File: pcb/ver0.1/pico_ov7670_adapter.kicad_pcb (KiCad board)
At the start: 2 copper layers, 95 x 46 mm, 12 parts, among them J1 Conn_02x06_Odd_Even, SW1 SW_Push, U1 CAMERA-OV7670, U2 RASPBERRY_PI_PICO_W

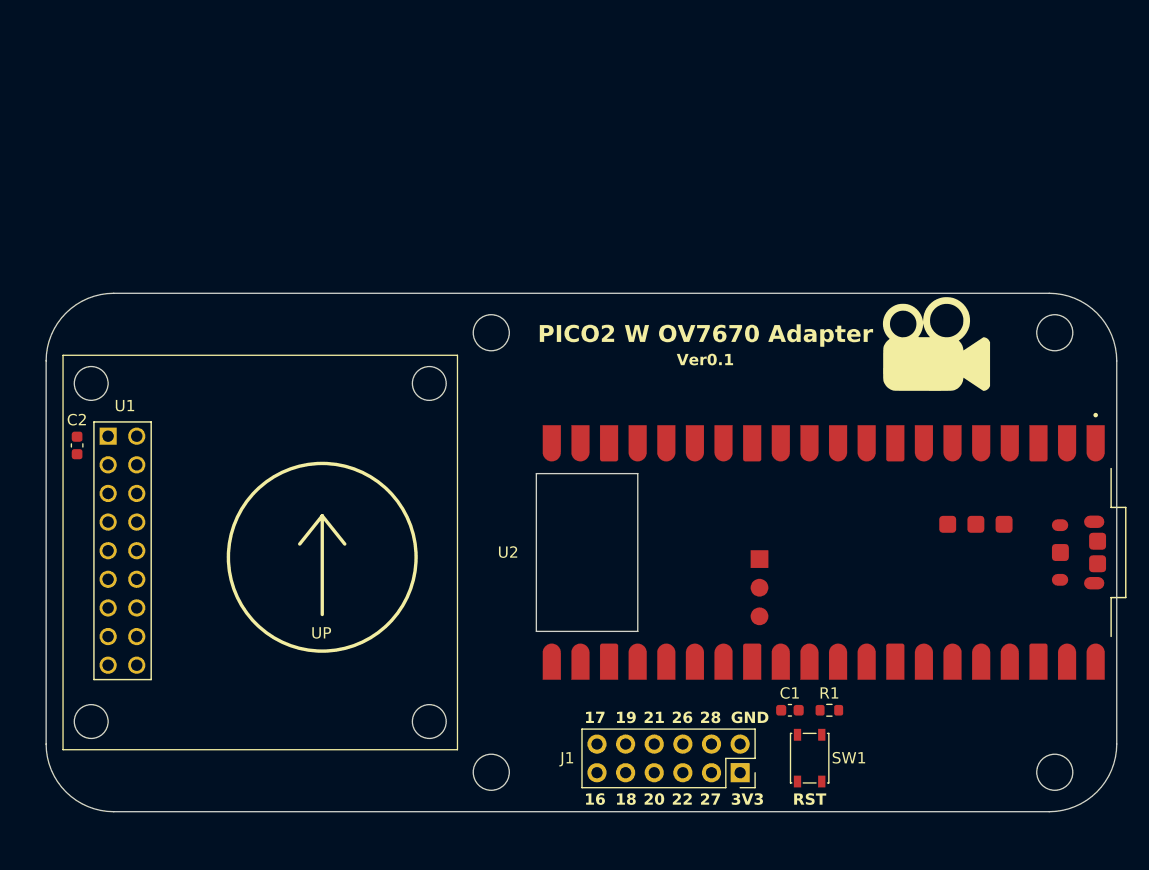
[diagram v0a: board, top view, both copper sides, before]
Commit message: footprints updated
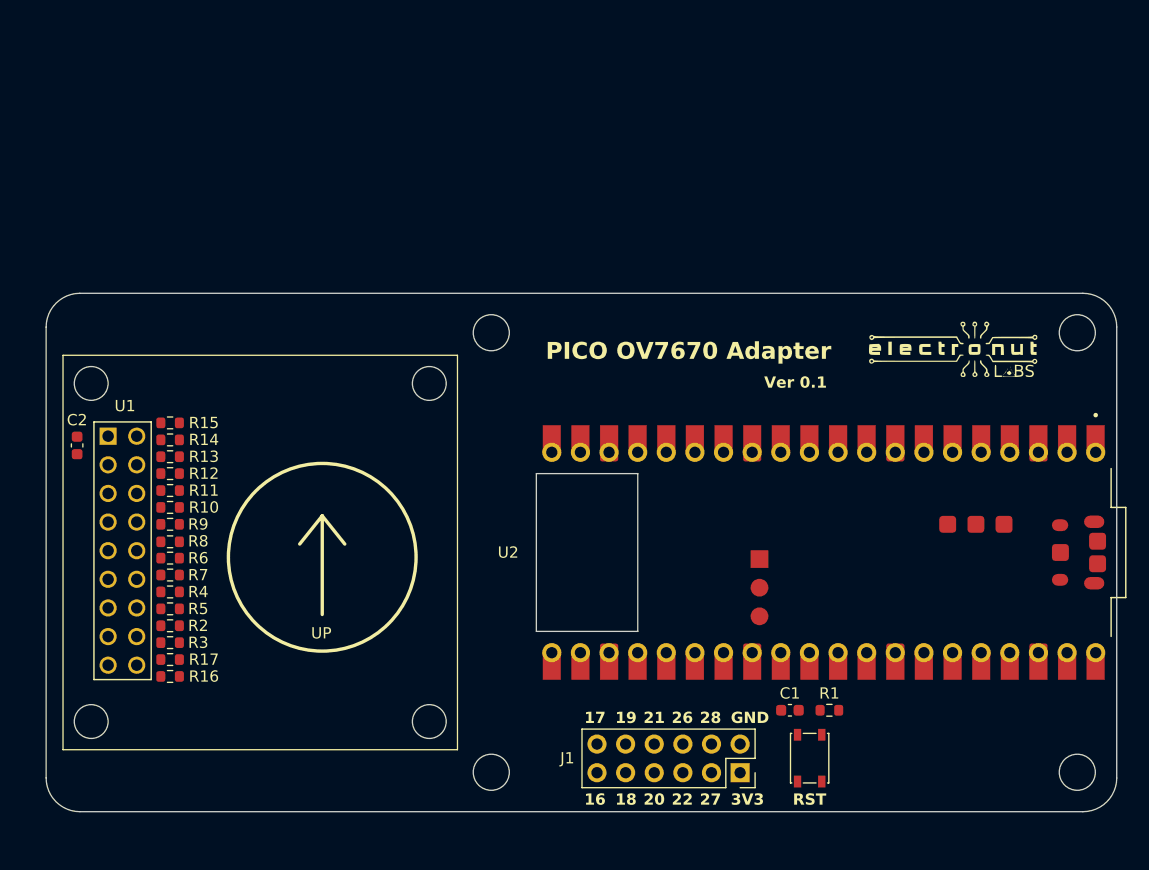
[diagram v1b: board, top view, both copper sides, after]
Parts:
- removed the G*** at (169.0, 78.5)
- added G***: LOGO, pico_ov7670_adapter:logo, F.Cu at (170.5, 79.0)
- added R10: 22R, Resistor_SMD:R_0603_1608Metric, F.Cu at (101.0, 93.0)
- added R11: 22R, Resistor_SMD:R_0603_1608Metric, F.Cu at (101.0, 91.5)
- added R12: 22R, Resistor_SMD:R_0603_1608Metric, F.Cu at (101.0, 90.0)
- added R13: 22R, Resistor_SMD:R_0603_1608Metric, F.Cu at (101.0, 88.5)
- added R14: 22R, Resistor_SMD:R_0603_1608Metric, F.Cu at (101.0, 87.0)
- added R15: 22R, Resistor_SMD:R_0603_1608Metric, F.Cu at (101.0, 85.5)
- added R16: 22R, Resistor_SMD:R_0603_1608Metric, F.Cu at (101.0, 108.0)
- added R17: 22R, Resistor_SMD:R_0603_1608Metric, F.Cu at (101.0, 106.5)
- added R2: 22R, Resistor_SMD:R_0603_1608Metric, F.Cu at (101.0, 103.5)
- added R3: 22R, Resistor_SMD:R_0603_1608Metric, F.Cu at (101.0, 105.0)
- added R4: 22R, Resistor_SMD:R_0603_1608Metric, F.Cu at (101.0, 100.5)
- added R5: 22R, Resistor_SMD:R_0603_1608Metric, F.Cu at (101.0, 102.0)
- added R6: 22R, Resistor_SMD:R_0603_1608Metric, F.Cu at (101.0, 97.5)
- added R7: 22R, Resistor_SMD:R_0603_1608Metric, F.Cu at (101.0, 99.0)
- added R8: 22R, Resistor_SMD:R_0603_1608Metric, F.Cu at (101.0, 96.0)
- added R9: 22R, Resistor_SMD:R_0603_1608Metric, F.Cu at (101.0, 94.5)
- moved H3 2.00 mm to (181.5, 77.5)
- moved H4 2.00 mm to (181.5, 116.5)
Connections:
- U2 pad 1: OV_D0_PICO_IO0 -> Net-(U2-UART0_TX/I2C0_SDA/SPI0_RX/GP0)
- U2 pad 10: OV_D7_PICO_IO7 -> Net-(U2-I2C1_SCL/SPI0_TX/GP7)
- U2 pad 11: OV_XCLK_PICO_IO8 -> Net-(U2-UART1_TX/I2C0_SDA/SPI1_RX/GP8)
- U2 pad 12: OV_PCLK_PICO_IO9 -> Net-(U2-UART1_RX/I2C0_SCL/SPI1_CSN/GP9)
- U2 pad 14: OV_VSYNC_PICO_IO10 -> Net-(U2-I2C1_SDA/SPI1_SCK/GP10)
- U2 pad 15: OV_HREF_PICO_IO11 -> Net-(U2-I2C1_SCL/SPI1_TX/GP11)
- U2 pad 16: OV_SDA_PICO_IO12_SDA -> Net-(U2-UART0_TX/I2C0_SDA/SPI1_RX/GP12)
- U2 pad 17: OV_SCL_PICO_IO13_SCL -> Net-(U2-UART0_RX/I2C0_SCL/SPI1_CSN/GP13)
- U2 pad 19: OV_RST_PICO_IO14 -> Net-(U2-I2C1_SDA/SPI1_SCK/GP14)
- U2 pad 2: OV_D1_PICO_IO1 -> Net-(U2-UART0_RX/I2C0_SCL/SPI0_CSN/GP1)
- U2 pad 20: OV_PWDWNPICO_IO15 -> Net-(U2-I2C1_SCL/SPI1_TX/GP15)
- U2 pad 4: OV_D2_PICO_IO2 -> Net-(U2-I2C1_SDA/SPI0_SCK/GP2)
- U2 pad 5: OV_D3_PICO_IO3 -> Net-(U2-I2C1_SCL/SPI0_TX/GP3)
- U2 pad 6: OV_D4_PICO_IO4 -> Net-(U2-UART1_TX/I2C0_SDA/SPI0_RX/GP4)
- U2 pad 7: OV_D5_PICO_IO5 -> Net-(U2-UART1_RX/I2C0_SCL/SPI0_CSN/GP5)
- U2 pad 9: OV_D6_PICO_IO6 -> Net-(U2-I2C1_SDA/SPI0_SCK/GP6)
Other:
- outline, holes or cut-outs redrawn
- board text added: "PICO OV7670 Adapter"
- board text added: "Ver 0.1"
- board text removed: "PICO2 W OV7670 Adapter"
- board text removed: "Ver0.1"

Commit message: layout updated
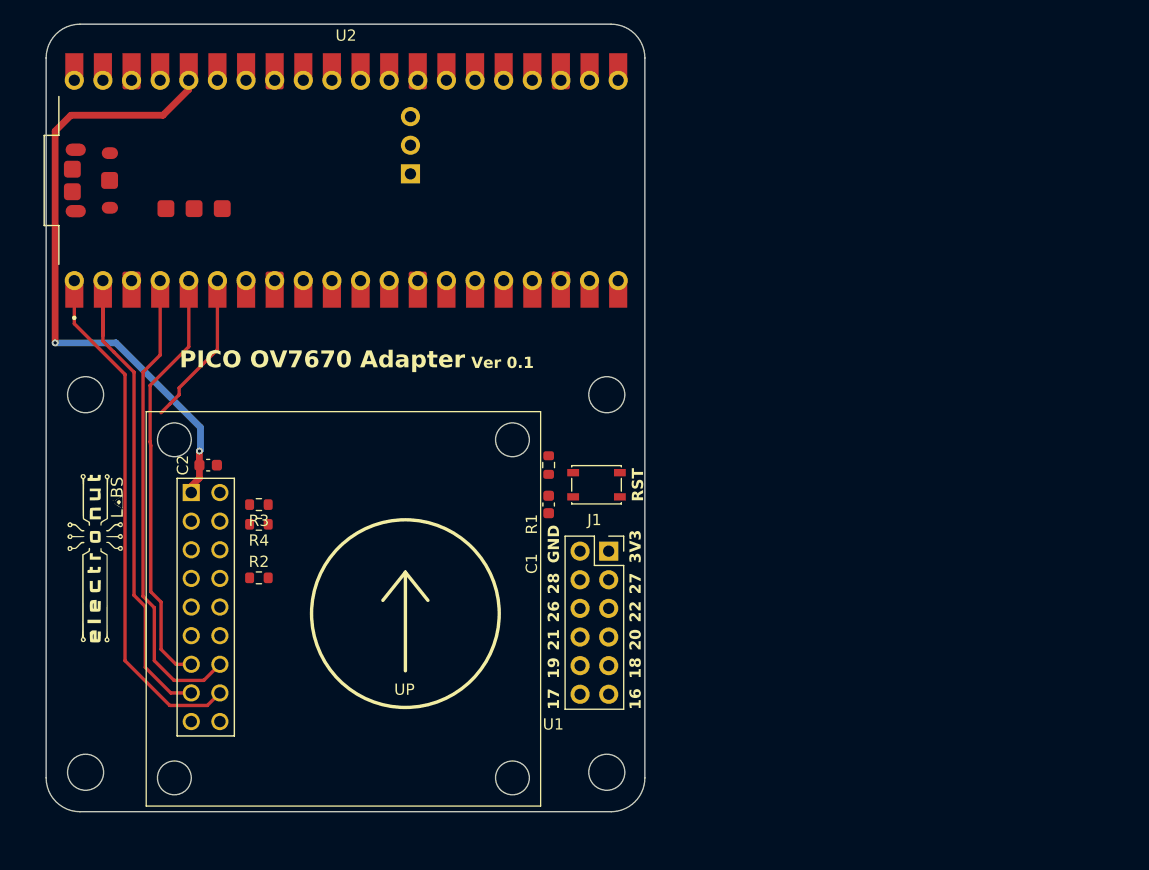
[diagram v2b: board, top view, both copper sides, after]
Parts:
- removed R10, R11, R12, R13, R14, R15, R16, R17, R5, R6, R7, R8, R9: 22R, Resistor_SMD:R_0603_1608Metric
- R3, R4: value 22R -> 10K
- moved H3 88.2 mm to (93.5, 83.0)
- moved H4 88.0 mm to (93.5, 116.5)
- moved G*** 78.3 mm to (94.4, 97.5), turned to 90 degrees
- moved U2 53.7 mm to (116.6, 64.0), turned to 90 degrees
- moved R1 33.1 mm to (134.6, 89.2), turned to -90 degrees
- moved SW1 30.8 mm to (138.8, 91.0), turned to 0 degrees
- moved C1 28.1 mm to (134.6, 92.7), turned to -90 degrees
- moved J1 22.9 mm to (139.9, 96.9), turned to 0 degrees
- moved R3 14.6 mm to (108.9, 92.8), turned to 180 degrees
- moved C2 11.8 mm to (104.4, 89.2), turned to 0 degrees
- moved H1 11.6 mm to (139.8, 83.0)
- moved H2 10.2 mm to (139.8, 116.5)
- moved R4 9.90 mm to (108.9, 94.5), turned to 180 degrees
- moved R2 8.95 mm to (108.9, 99.2)
- moved U1 8.91 mm to (116.4, 102.0)
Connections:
- R2 pad 1: OV_D0_PICO_IO0 -> OV_XCLK_PICO_IO8
- R2 pad 2: Net-(U2-UART0_TX/I2C0_SDA/SPI0_RX/GP0) -> Net-(U2-UART1_TX/I2C0_SDA/SPI1_RX/GP8)
- R3 pad 1: OV_D1_PICO_IO1 -> +3V3
- R3 pad 2: Net-(U2-UART0_RX/I2C0_SCL/SPI0_CSN/GP1) -> OV_SCL_PICO_IO13_SCL
- R4 pad 1: OV_D2_PICO_IO2 -> +3V3
- R4 pad 2: Net-(U2-I2C1_SDA/SPI0_SCK/GP2) -> OV_SDA_PICO_IO12_SDA
- U2 pad 1: Net-(U2-UART0_TX/I2C0_SDA/SPI0_RX/GP0) -> OV_D0_PICO_IO0
- U2 pad 10: Net-(U2-I2C1_SCL/SPI0_TX/GP7) -> OV_D7_PICO_IO7
- U2 pad 12: Net-(U2-UART1_RX/I2C0_SCL/SPI1_CSN/GP9) -> OV_PCLK_PICO_IO9
- U2 pad 14: Net-(U2-I2C1_SDA/SPI1_SCK/GP10) -> OV_VSYNC_PICO_IO10
- U2 pad 15: Net-(U2-I2C1_SCL/SPI1_TX/GP11) -> OV_HREF_PICO_IO11
- U2 pad 16: Net-(U2-UART0_TX/I2C0_SDA/SPI1_RX/GP12) -> OV_SDA_PICO_IO12_SDA
- U2 pad 17: Net-(U2-UART0_RX/I2C0_SCL/SPI1_CSN/GP13) -> OV_SCL_PICO_IO13_SCL
- U2 pad 19: Net-(U2-I2C1_SDA/SPI1_SCK/GP14) -> OV_RST_PICO_IO14
- U2 pad 2: Net-(U2-UART0_RX/I2C0_SCL/SPI0_CSN/GP1) -> OV_D1_PICO_IO1
- U2 pad 20: Net-(U2-I2C1_SCL/SPI1_TX/GP15) -> OV_PWDWNPICO_IO15
- U2 pad 4: Net-(U2-I2C1_SDA/SPI0_SCK/GP2) -> OV_D2_PICO_IO2
- U2 pad 5: Net-(U2-I2C1_SCL/SPI0_TX/GP3) -> OV_D3_PICO_IO3
- U2 pad 6: Net-(U2-UART1_TX/I2C0_SDA/SPI0_RX/GP4) -> OV_D4_PICO_IO4
- U2 pad 7: Net-(U2-UART1_RX/I2C0_SCL/SPI0_CSN/GP5) -> OV_D5_PICO_IO5
- U2 pad 9: Net-(U2-I2C1_SDA/SPI0_SCK/GP6) -> OV_D6_PICO_IO6
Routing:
- net +3V3: track 0.00 -> 56.0 mm, vias 0 -> 2
- net OV_D0_PICO_IO0: track 0.00 -> 45.3 mm
- net OV_D1_PICO_IO1: track 0.00 -> 45.0 mm
- net OV_D2_PICO_IO2: track 0.00 -> 41.1 mm
- net OV_D3_PICO_IO3: track 0.00 -> 37.0 mm
- net OV_D4_PICO_IO4: track 0.00 -> 13.8 mm
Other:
- board size 95 x 46 mm -> 53.1 x 69.9 mm

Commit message: basic routing completed
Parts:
- added C3: 0.1uF, Capacitor_SMD:C_0603_1608Metric, F.Cu at (136.2, 88.5)
- added R5: 10K, Resistor_SMD:R_0603_1608Metric, F.Cu at (134.8, 88.5)
- added SW2: SW_Push, Button_Switch_SMD:SW_SPST_PTS810, F.Cu at (140.0, 88.5)
- J1: value Conn_02x06_Odd_Even -> GPIO Header; footprint Connector_PinSocket_2.54mm:PinSocket_2x06_P2.54mm_Vertical -> Connector_PinHeader_2.54mm:PinHeader_2x05_P2.54mm_Vertical
- moved R1 5.76 mm to (134.8, 95.0), turned to 90 degrees
- moved J1 4.55 mm to (137.5, 100.7)
- moved SW1 3.94 mm to (140.0, 94.8)
- moved R4 3.00 mm to (109.0, 91.5)
- moved C1 2.80 mm to (136.2, 95.0)
- moved R3 1.75 mm to (109.0, 94.5)
- moved H2 0.35 mm to (140.0, 116.8)
- moved H3 0.35 mm to (93.2, 83.2)
- moved H4 0.35 mm to (93.2, 116.8)
- moved H1 0.25 mm to (140.0, 83.0)
- moved R2 0.12 mm to (109.0, 99.2)
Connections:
- net Net-(U2-~{RUN}) renamed /PICO_RESET
- J1 pad 10: /PICO_IO19 -> /PICO_IO27
- J1 pad 3: /PICO_IO27 -> GND
- J1 pad 4: /PICO_IO28 -> /PICO_IO19
- J1 pad 5: /PICO_IO22 -> /PICO_IO21
- J1 pad 6: /PICO_IO26 -> /PICO_IO20
- J1 pad 7: /PICO_IO20 -> /PICO_IO26
- J1 pad 8: /PICO_IO21 -> /PICO_IO22
- J1 pad 9: /PICO_IO18 -> /PICO_IO28
- R2 pad 2: Net-(U2-UART1_TX/I2C0_SDA/SPI1_RX/GP8) -> Net-(U2-UART0_TX/I2C0_SDA/SPI1_RX/GP12)
- U1 pad 18: OV_PWDWNPICO_IO15 -> OV_PWDWN_PICO_IO15
- U2 pad 11: Net-(U2-UART1_TX/I2C0_SDA/SPI1_RX/GP8) -> OV_SDA_PICO_IO12_SDA
- U2 pad 12: OV_PCLK_PICO_IO9 -> OV_SCL_PICO_IO13_SCL
- U2 pad 14: OV_VSYNC_PICO_IO10 -> OV_HREF_PICO_IO11
- U2 pad 15: OV_HREF_PICO_IO11 -> OV_VSYNC_PICO_IO10
- U2 pad 16: OV_SDA_PICO_IO12_SDA -> Net-(U2-UART0_TX/I2C0_SDA/SPI1_RX/GP12)
- U2 pad 17: OV_SCL_PICO_IO13_SCL -> OV_PCLK_PICO_IO9
- U2 pad 19: OV_RST_PICO_IO14 -> OV_PWDWN_PICO_IO15
- U2 pad 20: OV_PWDWNPICO_IO15 -> OV_RST_PICO_IO14
- U2 pad 21: /PICO_IO16 -> unconnected-(U2-UART0_TX/I2C0_SDA/SPI0_RX/GP16-Pad21)
- U2 pad 22: /PICO_IO17 -> unconnected-(U2-UART0_RX/I2C0_SCL/SPI0_CSN/GP17-Pad22)
- U2 pad 24: /PICO_IO18 -> /USER_Button
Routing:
- net +3V3: track 56.0 -> 162.8 mm, vias 2 -> 7
- net /PICO_IO28: track 0.00 -> 81.5 mm
- net /PICO_IO27: track 0.00 -> 77.8 mm
- net /PICO_IO26: track 0.00 -> 71.5 mm
- net /PICO_IO22: track 0.00 -> 71.4 mm
- net OV_RST_PICO_IO14: track 0.00 -> 66.9 mm
- net /PICO_RESET: track 0.00 -> 64.7 mm, vias 0 -> 1
- net /PICO_IO21: track 0.00 -> 63.1 mm
- net /PICO_IO20: track 0.00 -> 62.3 mm
- net OV_PWDWN_PICO_IO15: track 0.00 -> 61.9 mm
- net /PICO_IO19: track 0.00 -> 60.8 mm
- net OV_PCLK_PICO_IO9: track 0.00 -> 52.1 mm
- net OV_D6_PICO_IO6: track 0.00 -> 43.0 mm
- net OV_VSYNC_PICO_IO10: track 0.00 -> 42.2 mm
- net /USER_Button: track 0.00 -> 39.9 mm, vias 0 -> 1
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- added copper zone on B.Cu, net GND
- added copper zone on F.Cu, net GND
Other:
- outline, holes or cut-outs redrawn
- board text added: "PICO 2 OV7670 Adapter"
- board text added: "U.B"
- board text removed: "16"
- board text removed: "17"
- board text removed: "18"
- board text removed: "PICO OV7670 Adapter"
- board text removed: "UP"

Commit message: routing completed
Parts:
- turned R5 to 90 degrees
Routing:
- net OV_HREF_PICO_IO11: track 36.0 -> 39.3 mm
- net OV_VSYNC_PICO_IO10: track 42.2 -> 45.2 mm
- net /PICO_IO19: track 60.8 -> 58.1 mm
- net +3V3: track 162.8 -> 165.1 mm
- net Net-(U2-UART0_TX/I2C0_SDA/SPI1_RX/GP12): track 39.0 -> 40.7 mm
- net /PICO_RESET: track 64.7 -> 66.2 mm
- net /USER_Button: track 39.9 -> 41.4 mm
- net OV_RST_PICO_IO14: track 66.9 -> 68.4 mm
- net OV_D6_PICO_IO6: track 43.0 -> 41.9 mm
- net OV_PCLK_PICO_IO9: track 52.1 -> 53.0 mm
- net GND: vias 13 -> 9
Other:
- board text added: "USR"
- board text removed: "U.B"

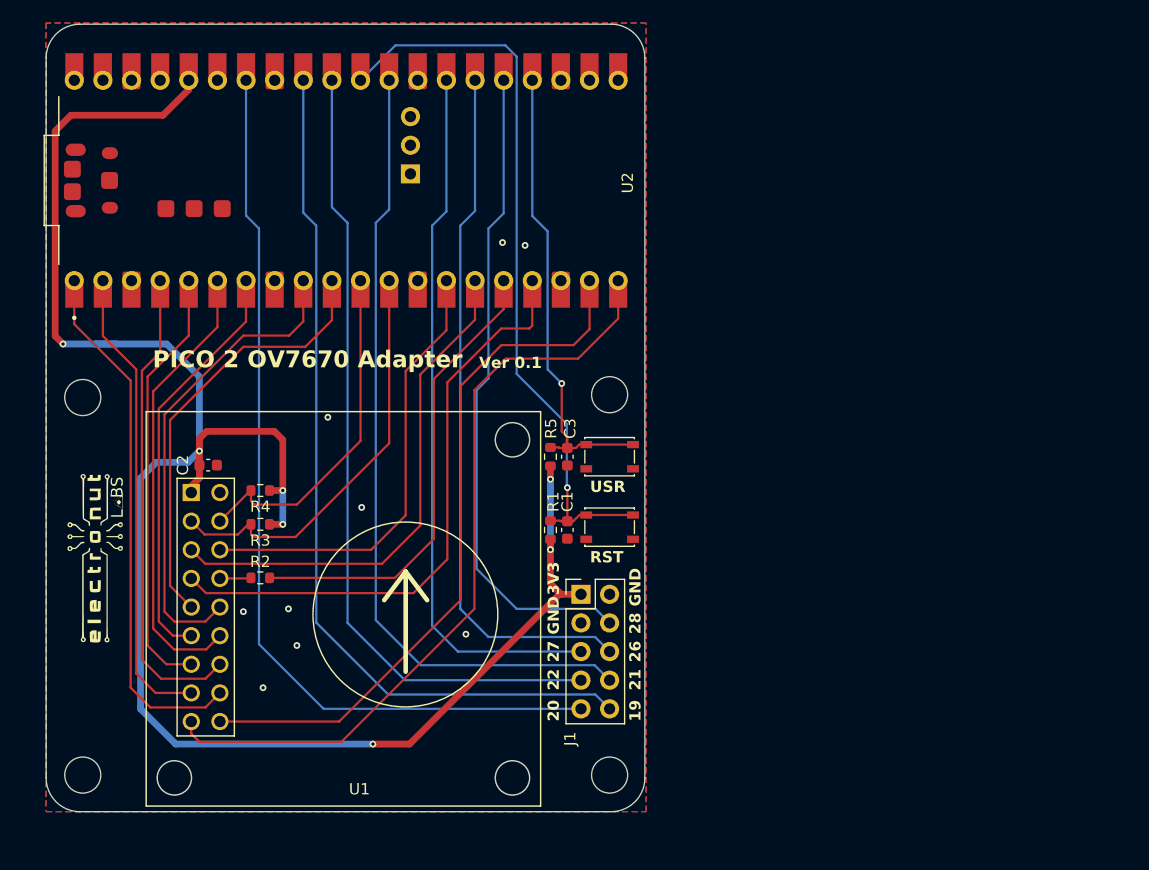
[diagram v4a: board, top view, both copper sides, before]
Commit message: art work updated in PCB
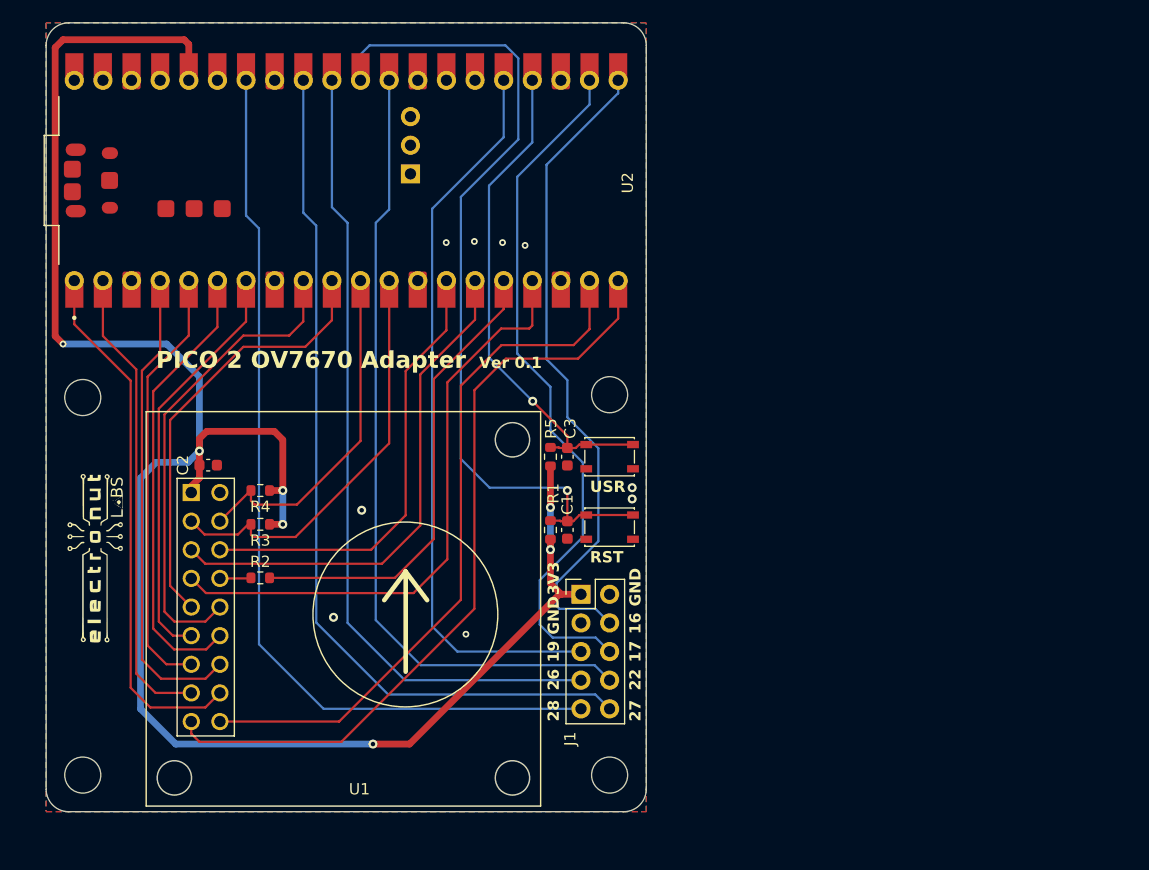
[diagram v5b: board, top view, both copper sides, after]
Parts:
- added G***: LOGO, pico_ov7670_adapter:art1, B.Cu at (101.9, 65.5)
- added G***: LOGO, pico_ov7670_adapter:art2, B.Cu at (134.0, 64.5)
- added G***: LOGO, pico_ov7670_adapter:art, B.Cu at (122.0, 101.5)
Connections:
- J1 pad 4: /PICO_IO19 -> /PICO_IO16
- J1 pad 5: /PICO_IO21 -> /PICO_IO19
- J1 pad 6: /PICO_IO20 -> /PICO_IO17
- U2 pad 21: unconnected-(U2-UART0_TX/I2C0_SDA/SPI0_RX/GP16-Pad21)_1 -> /PICO_IO16
- U2 pad 22: unconnected-(U2-UART0_RX/I2C0_SCL/SPI0_CSN/GP17-Pad22)_1 -> /PICO_IO17
- U2 pad 26: /PICO_IO20 -> unconnected-(U2-I2C0_SDA/GP20-Pad26)
- U2 pad 27: /PICO_IO21 -> unconnected-(U2-12C0_SCL/GP21-Pad27)_1
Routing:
- net /PICO_IO21: track 63.1 -> 0.00 mm
- net /PICO_IO20: track 62.3 -> 0.00 mm
- net /PICO_IO17: track 0.00 -> 62.1 mm
- net /PICO_IO16: track 0.00 -> 58.1 mm
- net /PICO_RESET: track 66.2 -> 75.6 mm
- net /PICO_IO19: track 58.1 -> 65.2 mm
- net +3V3: track 165.1 -> 169.4 mm
- net /USER_Button: track 41.4 -> 44.5 mm
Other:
- board size 53.1 x 69.9 mm -> 53.2 x 70 mm
- board text added: "16"
- board text added: "17"
- board text removed: "20"
- board text removed: "21"

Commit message: via stitching added
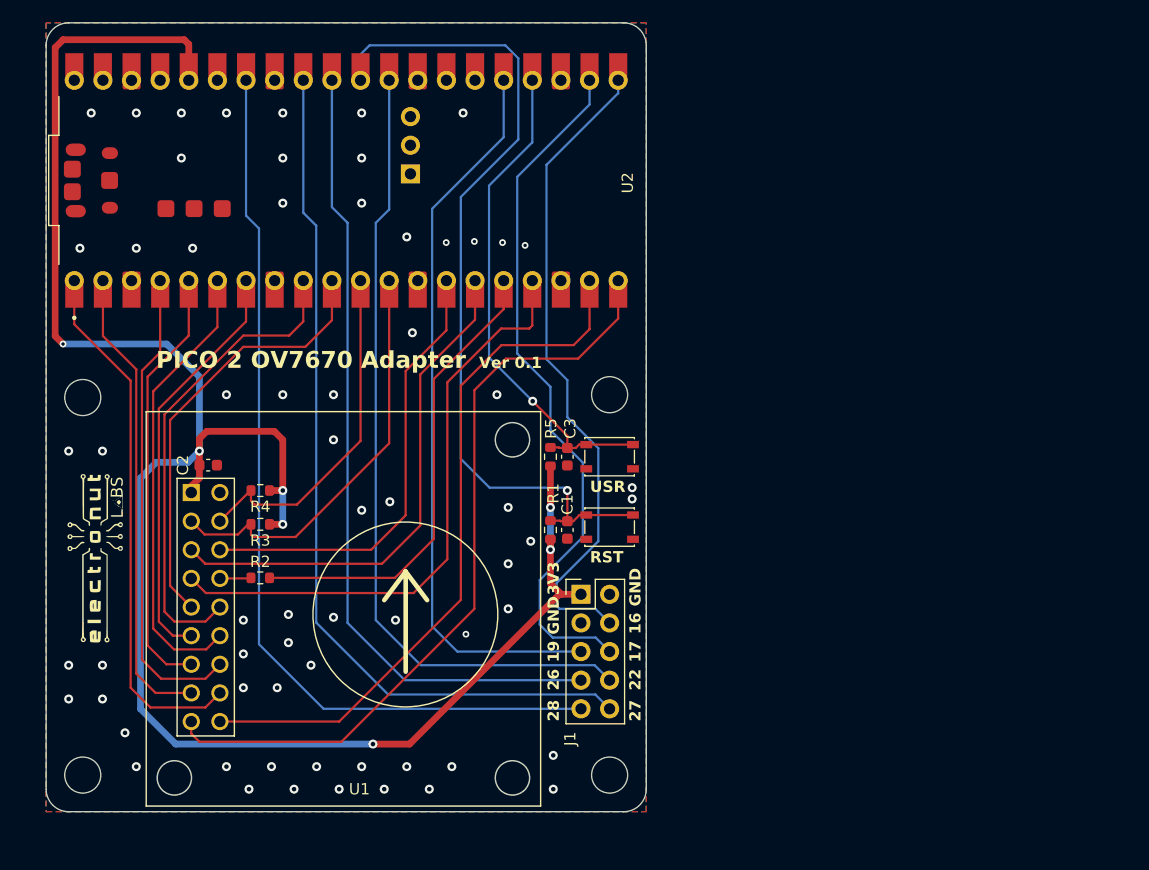
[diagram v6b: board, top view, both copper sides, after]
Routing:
- net GND: vias 9 -> 65
